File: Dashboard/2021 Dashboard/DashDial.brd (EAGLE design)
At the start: 88.9 x 66.3 mm, 31 parts, among them IC2 TLC5952DAP, J1 ESW-104-23-L-D, J2 ESW-104-23-L-D, U1 LOGIC SHIFTER, X2 SERVO

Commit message: Moved phat connector
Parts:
- removed C3: 0.1uF, SparkFun-Capacitors:0603
- removed U1: LOGIC SHIFTER, MC74VHC1GT125:SOT353
- removed X2: SERVO, con-wago-500:W237-103
- added SERVO: (no value), GTOR - Microfit Connector:43650-0315
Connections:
- removed net 5V: C3.1, U1.5
- removed net N$1: U1.4, X2.2
- net 7.4V: now also SERVO.P$1; no longer X2.3
- net GND: now also SERVO.P$3; no longer C3.2, U1.1, U1.3, X2.1
- net SERVO_CTRL: now also SERVO.P$2; no longer U1.2
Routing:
- net 5V: track 25.0 -> 0.00 mm
- net GND: track 129.6 -> 121.3 mm
- net N$1: track 8.13 -> 0.00 mm
- net SERVO_CTRL: track 147.3 -> 146.7 mm
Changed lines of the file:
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@@
 </autorouter>
 <elements>
-<element name="C3" library="SparkFun-Capacitors" package="0603" value="0.1uF" x="22.098" y="-9.652" smashed="yes" rot="MR90">
-<attribute name="NAME" x="22.733" y="-5.715" size="1.27" layer="26" rot="MR270"/>
-<attribute name="PROD_ID" value="CAP-00810" x="22.098" y="-9.652" size="1.778" layer="28" rot="MR90" display="off"/>
-<attribute name="VALUE" value="0.1uF" x="19.812" y="-11.811" size="1.27" layer="28" rot="MR90"/>
-</element>
-<element name="U1" library="MC74VHC1GT125" package="SOT353" value="LOGIC SHIFTER" x="25.273" y="-9.779" smashed="yes" rot="MR180">
-<attribute name="AVAILABILITY" value="Unavailable" x="60.833" y="6.731" size="1.778" layer="28" rot="MR180" display="off"/>
-<attribute name="DESCRIPTION" value=" Buffer, Non-Inverting 1 Element 1 Bit per Element 3-State Output SC-88A (SC-70-5/SOT-353) " x="60.833" y="6.731" size="1.778" layer="28" rot="MR180" display="off"/>
-<attribute name="MF" value="ON Semiconductor" x="60.833" y="6.731" size="1.778" layer="28" rot="MR180" display="off"/>
-<attribute name="MP" value="MC74VHC1GT125" x="60.833" y="6.731" size="1.778" layer="28" rot="MR180" display="off"/>
-<attribute name="NAME" x="26.459" y="-9.197" size="1.27" layer="26" rot="MR180"/>
-<attribute name="PACKAGE" value="SOT-353 ON Semiconductor" x="60.833" y="6.731" size="1.778" layer="28" rot="MR180" display="off"/>
-<attribute name="PRICE" value="None" x="60.833" y="6.731" size="1.778" layer="28" rot="MR180" display="off"/>
-<attribute name="VALUE" x="24.3" y="-7.206" size="1.27" layer="28" rot="MR180"/>
-</element>
-<element name="X2" library="con-wago-500" library_urn="urn:adsk.eagle:library:195" package="W237-103" package3d_urn="urn:adsk.eagle:package:10691/1" value="SERVO" x="21.209" y="-15.621" smashed="yes" rot="MR0">
-<attribute name="MF" value="" x="0.889" y="-24.511" size="1.778" layer="28" rot="MR0" display="off"/>
-<attribute name="MPN" value="237-103" x="0.889" y="-24.511" size="1.778" layer="28" rot="MR0" display="off"/>
-<attribute name="NAME" x="13.4328" y="-19.5272" size="1.27" layer="26" ratio="10" rot="MR0"/>
-<attribute name="OC_FARNELL" value="unknown" x="0.889" y="-24.511" size="1.778" layer="28" rot="MR0" display="off"/>
-<attribute name="OC_NEWARK" value="18M7116" x="0.889" y="-24.511" size="1.778" layer="28" rot="MR0" display="off"/>
-<attribute name="POPULARITY" value="5" x="0.889" y="-24.511" size="1.778" layer="28" rot="MR0" display="off"/>
-<attribute name="VALUE" x="13.5598" y="-20.9496" size="1.27" layer="28" ratio="10" rot="MR0"/>
-</element>
 <element name="D0" library="SparkFun-LED" package="LED_3MM" value="" x="-36.703" y="-19.431" smashed="yes">
 <attribute name="NAME" x="-36.703" y="-17.145" size="0.6096" layer="25" font="vector" ratio="20" align="bottom-center"/>
@@
 <attribute name="VALUE" x="-68.961" y="-73.66" size="0.6096" layer="27" font="vector" ratio="20" align="top-center"/>
 </element>
+<element name="SERVO" library="GTOR - Microfit Connector" package="43650-0315" value="" x="-66.802" y="-77.724" smashed="yes"/>
 </elements>
 <signals>
@@
 </signal>
 <signal name="GND">
-<contactref element="X2" pad="1"/>
-<contactref element="U1" pad="3"/>
-<contactref element="U1" pad="1"/>
-<contactref element="C3" pad="2"/>
 <polygon width="0.1524" layer="1" rank="2">
 <vertex x="-58.293" y="49.403"/>
@@
 <vertex x="60.579" y="49.403"/>
 </polygon>
-<wire x1="24.623" y1="-8.829" x2="22.125" y2="-8.829" width="0.1524" layer="16"/>
-<wire x1="22.125" y1="-8.829" x2="22.098" y2="-8.802" width="0.1524" layer="16"/>
 <polygon width="0.1524" layer="1" thermals="no">
 <vertex x="-20.066" y="-11.811"/>
@@
 <wire x1="-33.9344" y1="-19.7168" x2="-32.639" y2="-21.0122" width="0.8128" layer="16"/>
 <wire x1="-32.639" y1="-21.0122" x2="24.0728" y2="-21.0122" width="0.8128" layer="16"/>
-<wire x1="26.209" y1="-18.876" x2="26.209" y2="-16.911" width="0.8128" layer="16"/>
 <wire x1="24.0728" y1="-21.0122" x2="26.209" y2="-18.876" width="0.8128" layer="16"/>
 <wire x1="32.639" y1="-19.177" x2="27.178" y2="-19.177" width="0.8128" layer="16"/>
 <wire x1="27.178" y1="-19.177" x2="26.209" y2="-18.208" width="0.8128" layer="16"/>
-<wire x1="26.209" y1="-18.208" x2="26.209" y2="-16.911" width="0.8128" layer="16"/>
 <wire x1="36.83" y1="-4.191" x2="36.83" y2="-14.986" width="0.8128" layer="16"/>
 <wire x1="36.83" y1="-14.986" x2="32.639" y2="-19.177" width="0.8128" layer="16"/>
-<wire x1="24.623" y1="-8.829" x2="24.623" y2="-9.129" width="0.1524" layer="16"/>
-<wire x1="24.892" y1="-9.398" x2="25.654" y2="-9.398" width="0.1524" layer="16"/>
-<wire x1="25.654" y1="-9.398" x2="25.923" y2="-9.129" width="0.1524" layer="16"/>
-<wire x1="25.923" y1="-9.129" x2="25.923" y2="-8.829" width="0.1524" layer="16"/>
-<wire x1="24.623" y1="-9.129" x2="24.892" y2="-9.398" width="0.1524" layer="16"/>
 <wire x1="36.83" y1="-4.191" x2="37.8386" y2="-3.1824" width="0.1524" layer="16"/>
 <wire x1="37.8386" y1="-3.1824" x2="37.8386" y2="-1.23321875" width="0.1524" layer="16"/>
@@
 <wire x1="35.6034" y1="-1.45121875" x2="35.6034" y2="-2.1950375" width="0.1524" layer="16"/>
 <wire x1="34.6160375" y1="-3.1824" x2="29.91454375" y2="-3.1824" width="0.1524" layer="16"/>
-<wire x1="24.623" y1="-8.47394375" x2="24.623" y2="-8.829" width="0.1524" layer="16"/>
 <wire x1="37.8386" y1="-1.23321875" x2="37.24778125" y2="-0.6424" width="0.1524" layer="16"/>
 <wire x1="35.6034" y1="-2.1950375" x2="34.6160375" y2="-3.1824" width="0.1524" layer="16"/>
@@
 <contactref element="IC2" pad="29"/>
 <contactref element="IC2" pad="33"/>
+<contactref element="SERVO" pad="P$3"/>
+<wire x1="-72.771" y1="-72.644" x2="-69.802" y2="-77.724" width="0" layer="19" extent="1-1"/>
 <wire x1="-64.389" y1="-60.706" x2="-72.771" y2="-72.644" width="0" layer="19" extent="1-1"/>
 <wire x1="-60.6044" y1="-57.785" x2="-64.389" y2="-60.706" width="0" layer="19" extent="1-1"/>
 <wire x1="-34.29" y1="-4.191" x2="-60.6044" y2="-57.785" width="0" layer="19" extent="1-1"/>
+<wire x1="26.209" y1="-18.208" x2="26.209" y2="-18.876" width="0" layer="19" extent="16-16"/>
 </signal>
 <signal name="7.4V">
-<contactref element="X2" pad="3"/>
 <contactref element="J1" pad="03"/>
 <contactref element="J2" pad="03"/>
@@
 <wire x1="14.478" y1="-20.193" x2="16.256" y2="-18.415" width="0.4064" layer="16"/>
 <wire x1="16.256" y1="-18.415" x2="16.256" y2="-16.958" width="0.4064" layer="16"/>
-<wire x1="16.256" y1="-16.958" x2="16.209" y2="-16.911" width="0.4064" layer="16"/>
 <wire x1="-32.512" y1="-3.429" x2="-32.512" y2="-10.5324375" width="0.4064" layer="16"/>
 <wire x1="36.83" y1="-1.651" x2="35.56" y2="-2.921" width="0.4064" layer="16"/>
@@
 <wire x1="35.56" y1="-2.921" x2="35.56" y2="-14.097" width="0.4064" layer="16"/>
 <wire x1="21.717" y1="-19.685" x2="17.526" y2="-19.685" width="0.4064" layer="16"/>
+<contactref element="SERVO" pad="P$1"/>
+<wire x1="-34.29" y1="-1.651" x2="-63.802" y2="-77.724" width="0" layer="19" extent="1-1"/>
 </signal>
 <signal name="SIN">
@@
 </signal>
 <signal name="SERVO_CTRL">
-<contactref element="U1" pad="2"/>
 <contactref element="J1" pad="02"/>
 <contactref element="J2" pad="02"/>
@@
 <wire x1="29.337" y1="-4.191" x2="25.8445" y2="-7.6835" width="0.1524" layer="16"/>
 <wire x1="25.8445" y1="-7.6835" x2="25.273" y2="-8.255" width="0.1524" layer="16"/>
-<wire x1="25.273" y1="-8.255" x2="25.273" y2="-8.829" width="0.1524" layer="16"/>
 <wire x1="-36.83" y1="-4.191" x2="-39.751" y2="-1.27" width="0.1524" layer="16"/>
 <wire x1="-39.751" y1="-1.27" x2="-39.751" y2="2.97105625" width="0.1524" layer="16"/>
@@
 <wire x1="20.828" y1="-11.811" x2="24.511" y2="-11.811" width="0.1524" layer="16"/>
 <wire x1="25.273" y1="-10.414" x2="26.416" y2="-9.271" width="0.1524" layer="16"/>
-</signal>
-<signal name="N$1">
-<contactref element="U1" pad="4"/>
-<contactref element="X2" pad="2"/>
-<wire x1="25.923" y1="-10.729" x2="25.923" y2="-12.197" width="0.1524" layer="16"/>
-<wire x1="25.923" y1="-12.197" x2="21.209" y2="-16.911" width="0.1524" layer="16"/>
-</signal>
-<signal name="5V">
-<contactref element="C3" pad="1"/>
-<contactref element="U1" pad="5"/>
-<wire x1="22.098" y1="-10.502" x2="22.325" y2="-10.729" width="0.1524" layer="16"/>
-<wire x1="22.325" y1="-10.729" x2="24.623" y2="-10.729" width="0.1524" layer="16"/>
-<wire x1="35.2986" y1="-0.6424" x2="35.2986" y2="-2.06878125" width="0.1524" layer="16"/>
-<wire x1="35.2986" y1="-2.06878125" x2="34.70038125" y2="-2.667" width="0.1524" layer="16"/>
-<wire x1="25.527" y1="-2.667" x2="20.701" y2="-7.493" width="0.1524" layer="16"/>
-<wire x1="20.701" y1="-7.493" x2="20.701" y2="-10.033" width="0.1524" layer="16"/>
-<wire x1="21.17" y1="-10.502" x2="22.098" y2="-10.502" width="0.1524" layer="16"/>
-<wire x1="34.70038125" y1="-2.667" x2="25.527" y2="-2.667" width="0.1524" layer="16"/>
-<wire x1="20.701" y1="-10.033" x2="21.17" y2="-10.502" width="0.1524" layer="16"/>
+<contactref element="SERVO" pad="P$2"/>
+<wire x1="-36.83" y1="-4.191" x2="-66.802" y2="-77.724" width="0" layer="19" extent="1-1"/>
 </signal>
 <signal name="+3V3">
@@
 which will not be processed correctly with this version.
 </note>
-<note version="8.2" severity="warning">
-Since Version 8.2, EAGLE supports online libraries. The ids
-of those online libraries will not be understood (or retained)
-with this version.
-</note>
-<note version="8.3" severity="warning">
-Since Version 8.3, EAGLE supports URNs for individual library
-assets (packages, symbols, and devices). The URNs of those assets
-will not be understood (or retained) with this version.
-</note>
-<note version="8.3" severity="warning">
-Since Version 8.3, EAGLE supports the association of 3D packages
-with devices in libraries, schematics, and board files. Those 3D
-packages will not be understood (or retained) with this version.
-</note>
 </compatibility>

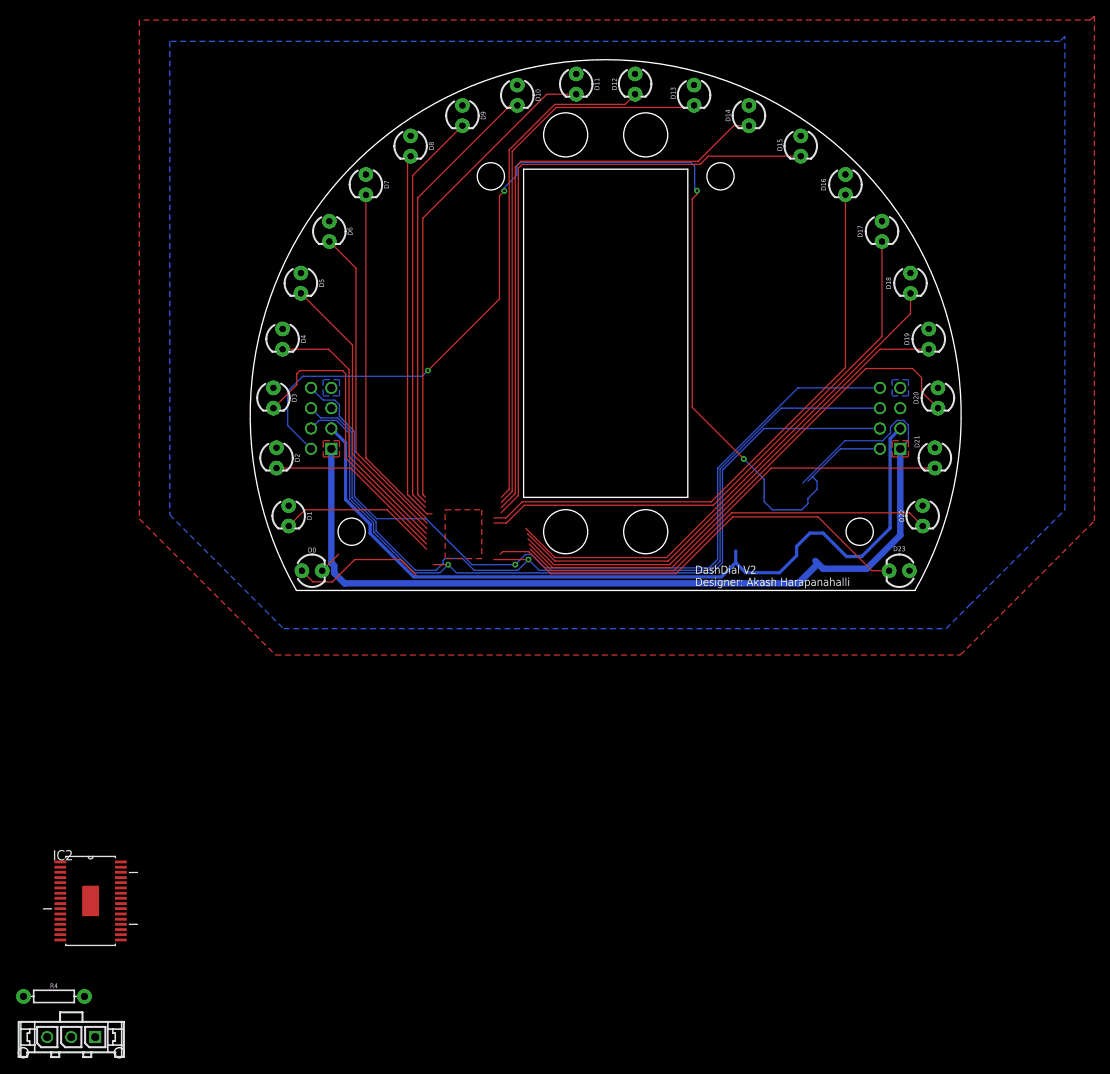
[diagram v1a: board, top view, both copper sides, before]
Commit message: More work done to dash hub and dial, gps board added
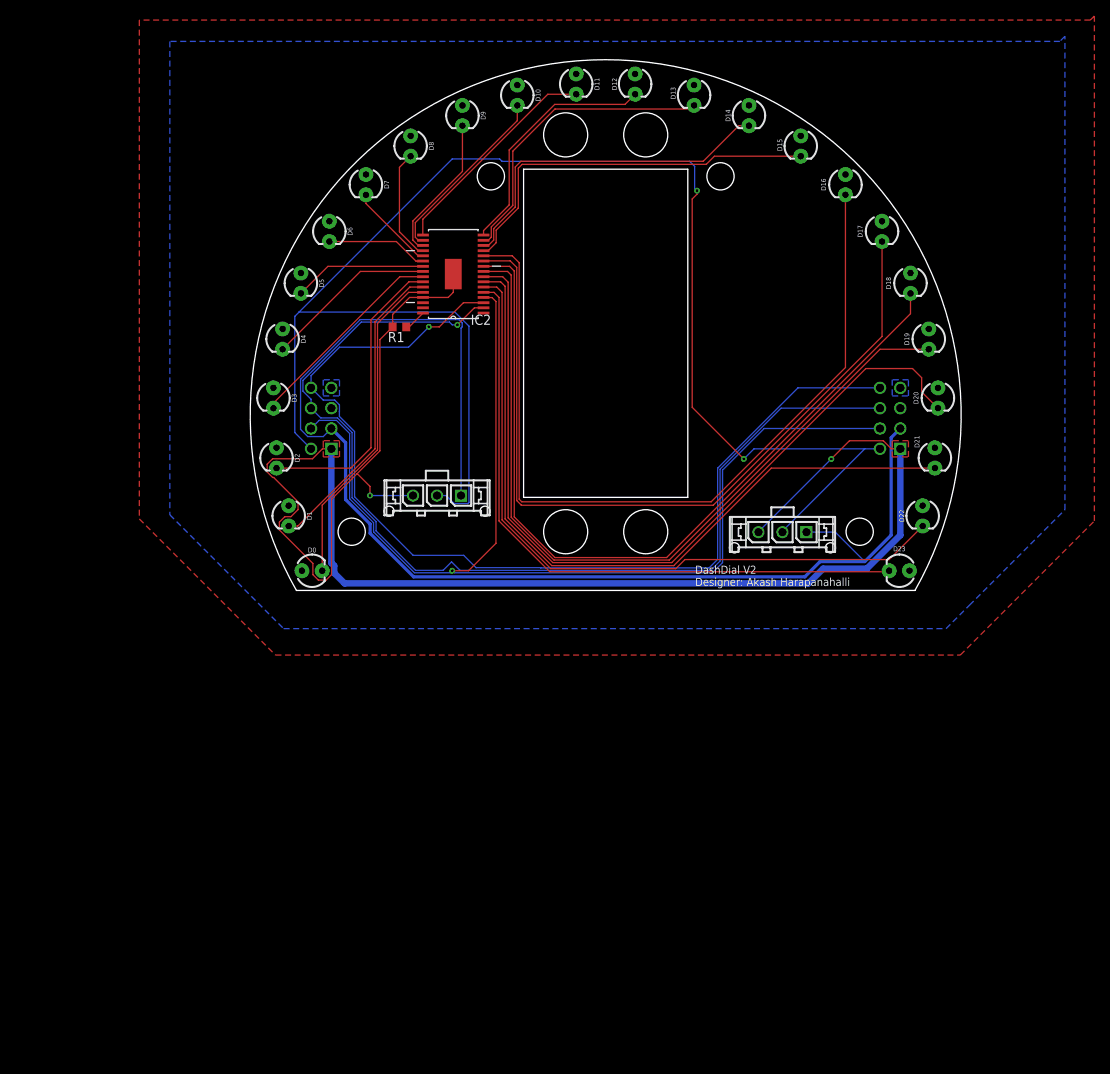
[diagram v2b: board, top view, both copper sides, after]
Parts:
- removed R4: 3k, SparkFun-Resistors:AXIAL-0.3
- added R1: (no value), GTOR - Passive Components:R0603
- added SERVO1: (no value), GTOR - Microfit Connector:43650-0315
- moved SERVO 109.0 mm to (22.1, -14.6)
- moved IC2 90.5 mm to (-19.1, 17.7), turned to 180 degrees
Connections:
- net 7.4V: now also SERVO1.P$1
- net GND: now also R1.2, SERVO1.P$3; no longer R4.P$1
- net N$31: now also R1.1; no longer R4.P$2
- net SERVO_CTRL: now also SERVO1.P$2
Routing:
- net GND: track 121.3 -> 209.0 mm, vias 0 -> 2
- net 7.4V: track 103.5 -> 163.3 mm
- net SERVO_CTRL: track 146.7 -> 196.2 mm, vias 4 -> 2
- net OUT23: track 2.89 -> 41.1 mm
- net OUT5: track 64.8 -> 101.6 mm
- net OUT4: track 62.5 -> 99.2 mm
- net LAT: track 101.8 -> 138.2 mm
- net OUT3: track 65.8 -> 102.0 mm
- net OUT2: track 57.1 -> 93.2 mm
- net OUT1: track 53.8 -> 88.3 mm
- net OUT12: track 60.6 -> 27.6 mm
- net OUT13: track 55.7 -> 22.9 mm
- net OUT15: track 46.5 -> 13.9 mm
- net OUT14: track 51.0 -> 18.4 mm
- net OUT16: track 43.5 -> 11.0 mm
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
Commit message: Fixed the dashhub #everything
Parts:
- SERVO, SERVO1: device GTOR - Microfit Connector:43650-0315 -> GTOR - Microfit Connector:43650-0300
- moved SERVO 18.1 mm to (20.8, 3.43)
- moved SERVO1 13.5 mm to (-20.8, 3.43)
- moved R1 0.25 mm to (-25.8, 10.8)
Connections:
- removed net +3V3: IC2.31
- removed net N$30: IC2.1
- net 3.3V: now also IC2.31
- net GND: now also IC2.1
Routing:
- net GND: track 209.0 -> 169.0 mm, vias 2 -> 0
- net SERVO_CTRL: track 196.2 -> 166.1 mm, vias 2 -> 0
- net 7.4V: track 163.3 -> 155.5 mm
- net 3.3V: track 0.00 -> 3.56 mm, vias 0 -> 2
- net SIN: track 131.5 -> 129.9 mm
- net LAT: track 138.2 -> 137.5 mm

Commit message: Design review fixes
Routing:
- net GND: track 169.0 -> 197.1 mm, vias 0 -> 3
- net 3.3V: track 3.56 -> 31.5 mm, vias 2 -> 5
- net SERVO_CTRL: track 166.1 -> 139.7 mm, vias 0 -> 1
- net 7.4V: track 155.5 -> 145.4 mm, vias 0 -> 3
- net OUT20: track 25.9 -> 29.0 mm
- net LAT: track 137.5 -> 135.4 mm
- net SCLK: track 128.9 -> 127.5 mm
- net SIN: track 129.9 -> 128.7 mm
- net OUT6: track 100.2 -> 100.8 mm
- net OUT7: track 103.8 -> 104.4 mm
- net OUT5: track 101.6 -> 102.2 mm
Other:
- board text added: "DashDial V3 Designer: Param Pithadia"
- board text removed: "DashDial V2 Designer: Akash Harapanahalli"

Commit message: Added resistor values to dashhub and board
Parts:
- R_IREF: value (none) -> 2.4k
- renumbered R1 to R_IREF
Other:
- board text added: "SERVO_CTRL"
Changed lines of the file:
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@@
 <text x="-40.005" y="-10.414" size="1.27" layer="26" rot="MR0">+</text>
 <text x="-38.608" y="-18.542" size="1.27" layer="26" rot="MR0">+</text>
+<text x="19.304" y="9.779" size="0.381" layer="25">SERVO_CTRL</text>
+<text x="-22.352" y="9.271" size="0.381" layer="25">SERVO_CTRL</text>
 </plain>
 <attributes>
@@
 <element name="J1" library="ESW-104-23-L-D" package="SAMTEC_ESW-104-23-L-D" value="ESW-104-23-L-D" x="36.83" y="-4.191" smashed="yes" rot="MR270">
 <attribute name="MANUFACTURER" value="Samtec Inc." x="36.83" y="-4.191" size="1.778" layer="28" rot="MR270" display="off"/>
-<attribute name="NAME" x="31.835" y="5.954" size="1.27" layer="26" rot="MR270"/>
+<attribute name="NAME" x="34.248" y="-7.254" size="1.27" layer="26" rot="MR270"/>
 <attribute name="PARTREV" value="R" x="36.83" y="-4.191" size="1.778" layer="28" rot="MR270" display="off"/>
 <attribute name="STANDARD" value="Manufacturer Recommendations" x="36.83" y="-4.191" size="1.778" layer="28" rot="MR270" display="off"/>
@@
 <attribute name="PARTREV" value="R" x="-34.29" y="-4.191" size="1.778" layer="28" rot="MR270" display="off"/>
 <attribute name="STANDARD" value="Manufacturer Recommendations" x="-34.29" y="-4.191" size="1.778" layer="28" rot="MR270" display="off"/>
-<attribute name="VALUE" x="-30.585" y="5.954" size="1.27" layer="28" rot="MR270"/>
+<attribute name="VALUE" x="-31.22" y="5.954" size="1.27" layer="28" rot="MR270"/>
 </element>
 <element name="IC2" library="GTOR - Active Components" package="SOP65P810X120-33N" value="TLC5952DAP" x="-19.05" y="17.653" smashed="yes" rot="R180">
@@
 <attribute name="MOUSER_PRICE-STOCK" value="https://www.mouser.co.uk/ProductDetail/Texas-Instruments/TLC5952DAP?qs=IK5e5L0zOXhuADcxoTQ%252BEg%3D%3D" x="-19.05" y="17.653" size="1.778" layer="27" rot="R180" display="off"/>
 <attribute name="NAME" x="-15.5956" y="11.938" size="1.27" layer="25" rot="R180" align="center"/>
-<attribute name="VALUE" x="-15.5956" y="26.543" size="1.27" layer="27" rot="R180" align="center"/>
+<attribute name="VALUE" x="-18.8976" y="24.384" size="1.27" layer="27" rot="R180" align="center"/>
 </element>
 <element name="SERVO" library="GTOR - Microfit Connector" package="43650-0300" value="" x="20.828" y="3.429" smashed="yes"/>
-<element name="R1" library="GTOR - Passive Components" package="R0603" package3d_urn="urn:adsk.eagle:package:23555/3" value="" x="-25.781" y="10.795" smashed="yes" rot="R180">
+<element name="R_IREF" library="GTOR - Passive Components" package="R0603" package3d_urn="urn:adsk.eagle:package:23555/3" value="2.4k" x="-25.781" y="10.795" smashed="yes" rot="R180">
 <attribute name="NAME" x="-25.146" y="10.16" size="1.27" layer="25" rot="R180"/>
 <attribute name="POPULARITY" value="77" x="-25.781" y="10.795" size="1.778" layer="27" rot="R180" display="off"/>
@@
 <contactref element="IC2" pad="33"/>
 <contactref element="SERVO" pad="P$3"/>
-<contactref element="R1" pad="2"/>
+<contactref element="R_IREF" pad="2"/>
 <wire x1="32.639" y1="-19.177" x2="36.83" y2="-14.986" width="0.8128" layer="16"/>
 <wire x1="-24.511" y1="14.732" x2="-22.8346" y2="14.732" width="0.1524" layer="1"/>
@@
 <signal name="N$31">
 <contactref element="IC2" pad="32"/>
-<contactref element="R1" pad="1"/>
+<contactref element="R_IREF" pad="1"/>
 <wire x1="-22.8346" y1="12.7762" x2="-24.8158" y2="10.795" width="0.1524" layer="1"/>
 <wire x1="-24.8158" y1="10.795" x2="-24.931" y2="10.795" width="0.1524" layer="1"/>
